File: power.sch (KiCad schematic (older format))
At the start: 38 parts, among them J1 USB_B_Mini, U1 USBLC6-2SC6, U2 BQ24190, U4 LP38691SD-3.3

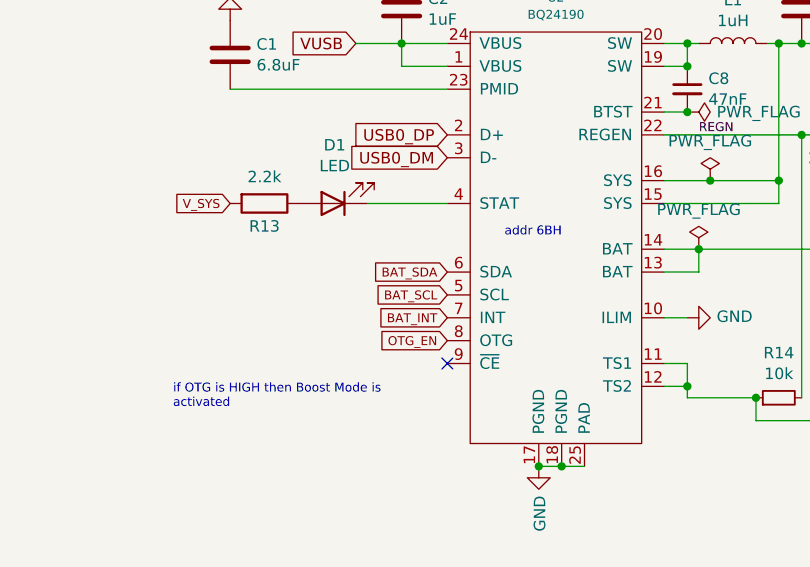
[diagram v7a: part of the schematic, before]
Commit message: Move touchscreen to user i2c with jumpers
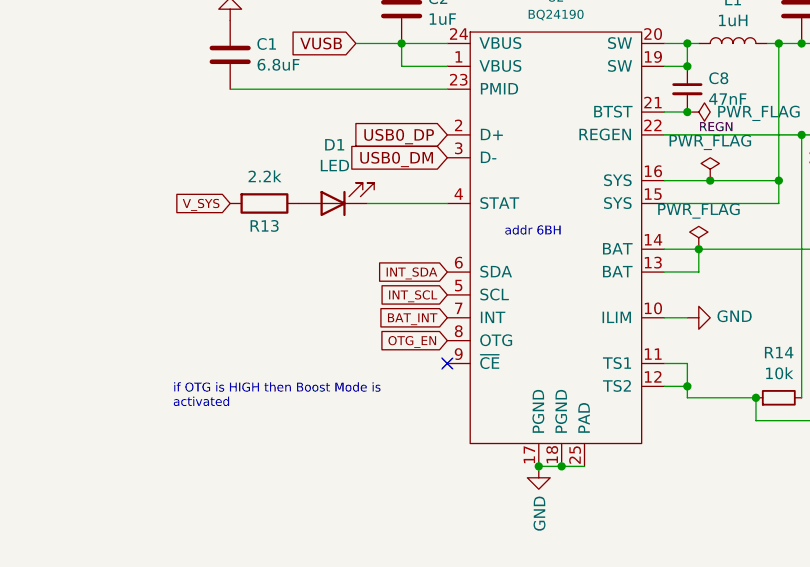
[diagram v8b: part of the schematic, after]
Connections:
- net BAT_SCL renamed INT_SCL
- net BAT_SDA renamed INT_SDA
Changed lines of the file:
@@
 USB0_ID
 Text GLabel 6250 4750 0    39   Input ~ 0
-BAT_SDA
+INT_SDA
 Text GLabel 6250 4850 0    39   Input ~ 0
-BAT_SCL
+INT_SCL
 Text GLabel 6250 4950 0    39   Input ~ 0
 BAT_INT
